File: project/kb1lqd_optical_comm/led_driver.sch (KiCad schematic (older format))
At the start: 0 parts

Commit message: Updated with better values and text.
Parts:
- added C?: 3.9n, symbol Device:C
- added Q?: PMBT2222AYS, Package_TO_SOT_SMD:SOT-363_SC-70-6, symbol Transistor_BJT:PMBT2222AYS
- added R?: 10k, symbol Device:R_US
- added R? (x2): 3.2k, symbol Device:R_US
- added R?: 1k, symbol Device:R_US
- added R?: 140, symbol Device:R_US
- added U?: AD8648, symbol kb1lqd_optical_comm:AD8648
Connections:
- net labels added: +5V, GND
- wire segments 0 -> 20
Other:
- note added: "1.2V Reference"
- note added: "LED DRIVE OUTPUT"
- note added: "UPDATED TO PMBF170 NMOS"
- note added: "fc(3dB)= x"
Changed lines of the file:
@@
 $Descr A4 11693 8268
 encoding utf-8
-Sheet 3 4
+Sheet 2 4
 Title ""
 Date ""
@@
 Comment4 ""
 $EndDescr
-Text HLabel 1800 2400 0    50   Input Italic 10
+Text HLabel 2050 3750 0    50   Input Italic 10
 AUDIO_INPUT
-Text HLabel 7050 2350 0    50   Input Italic 10
+Text HLabel 6950 2100 2    50   Input Italic 10
 LED_DRV
-Text HLabel 7050 2650 0    50   Input Italic 10
+Text HLabel 6950 2500 2    50   Input Italic 10
 LED_RTN
+$Comp
+L kb1lqd_optical_comm:AD8648 U?
+U 2 1 5F682513
+P 4900 3250
+F 0 "U?" H 5550 3283 50  0000 C CNN
+F 1 "AD8648" H 5550 3374 50  0000 C CNN
+F 2 "" H 4900 3250 50  0001 C CNN
+F 3 "" H 4900 3250 50  0001 C CNN
+	2    4900 3250
+	1    0    0    1
+$EndComp
+$Comp
+L Device:R_US R?
+U 1 1 5F6830F5
+P 2500 3750
+F 0 "R?" V 2295 3750 50  0000 C CNN
+F 1 "10k" V 2386 3750 50  0000 C CNN
+F 2 "" V 2540 3740 50  0001 C CNN
+F 3 "~" H 2500 3750 50  0001 C CNN
+	1    2500 3750
+	0    1    1    0
+$EndComp
+$Comp
+L Device:R_US R?
+U 1 1 5F684468
+P 4350 2950
+F 0 "R?" H 4418 2996 50  0000 L CNN
+F 1 "3.2k" H 4418 2905 50  0000 L CNN
+F 2 "" V 4390 2940 50  0001 C CNN
+F 3 "~" H 4350 2950 50  0001 C CNN
+	1    4350 2950
+	1    0    0    -1
+$EndComp
+Wire Wire Line
+	2350 3750 2050 3750
+Wire Wire Line
+	2650 3750 2900 3750
+Wire Wire Line
+	2900 3750 2900 3850
+Wire Wire Line
+	2900 4150 2900 4450
+Wire Wire Line
+	4350 3100 4350 3750
+Wire Wire Line
+	4350 4350 4350 4450
+Wire Wire Line
+	4350 2800 4350 2650
+$Comp
+L Device:R_US R?
+U 1 1 5F684893
+P 4350 4200
+F 0 "R?" H 4418 4246 50  0000 L CNN
+F 1 "1k" H 4418 4155 50  0000 L CNN
+F 2 "" V 4390 4190 50  0001 C CNN
+F 3 "~" H 4350 4200 50  0001 C CNN
+	1    4350 4200
+	1    0    0    -1
+$EndComp
+$Comp
+L power:GND #PWR?
+U 1 1 5F68C24A
+P 6950 4450
+F 0 "#PWR?" H 6950 4200 50  0001 C CNN
+F 1 "GND" H 6955 4277 50  0000 C CNN
+F 2 "" H 6950 4450 50  0001 C CNN
+F 3 "" H 6950 4450 50  0001 C CNN
+	1    6950 4450
+	1    0    0    -1
+$EndComp
+$Comp
+L power:GND #PWR?
+U 1 1 5F68C502
+P 2900 4450
+F 0 "#PWR?" H 2900 4200 50  0001 C CNN
+F 1 "GND" H 2905 4277 50  0000 C CNN
+F 2 "" H 2900 4450 50  0001 C CNN
+F 3 "" H 2900 4450 50  0001 C CNN
+	1    2900 4450
+	1    0    0    -1
+$EndComp
+$Comp
+L power:+5V #PWR?
+U 1 1 5F68CB23
+P 4350 2650
+F 0 "#PWR?" H 4350 2500 50  0001 C CNN
+F 1 "+5V" H 4365 2823 50  0000 C CNN
+F 2 "" H 4350 2650 50  0001 C CNN
+F 3 "" H 4350 2650 50  0001 C CNN
+	1    4350 2650
+	1    0    0    -1
+$EndComp
+Connection ~ 2900 3750
+Connection ~ 4350 3750
+Wire Wire Line
+	4350 3750 4350 4050
+Wire Wire Line
+	4350 3750 5250 3750
+$Comp
+L Transistor_BJT:PMBT2222AYS Q?
+U 1 1 5F6932D5
+P 6850 3650
+F 0 "Q?" H 7041 3696 50  0000 L CNN
+F 1 "PMBT2222AYS" H 7041 3605 50  0000 L CNN
+F 2 "Package_TO_SOT_SMD:SOT-363_SC-70-6" H 7050 3750 50  0001 C CNN
+F 3 "https://assets.nexperia.com/documents/data-sheet/PMBT2222AYS.pdf" H 6850 3650 50  0001 C CNN
+	1    6850 3650
+	1    0    0    -1
+$EndComp
+Wire Wire Line
+	5850 3650 6650 3650
+Wire Wire Line
+	6950 3450 6950 2900
+Wire Wire Line
+	6950 2900 5850 2900
+Wire Wire Line
+	5050 2900 5050 3550
+Wire Wire Line
+	5050 3550 5250 3550
+$Comp
+L Device:R_US R?
+U 1 1 5F6951A2
+P 5700 2900
+F 0 "R?" V 5495 2900 50  0000 C CNN
+F 1 "3.2k" V 5586 2900 50  0000 C CNN
+F 2 "" V 5740 2890 50  0001 C CNN
+F 3 "~" H 5700 2900 50  0001 C CNN
+	1    5700 2900
+	0    1    1    0
+$EndComp
+Wire Wire Line
+	5550 2900 5050 2900
+Text Notes 7050 3400 0    50   Italic 10
+UPDATED TO PMBF170 NMOS
+Wire Wire Line
+	6950 2900 6950 2500
+Connection ~ 6950 2900
+Wire Wire Line
+	6950 2100 6950 1550
+$Comp
+L power:+5V #PWR?
+U 1 1 5F69BF76
+P 6950 1550
+F 0 "#PWR?" H 6950 1400 50  0001 C CNN
+F 1 "+5V" H 6965 1723 50  0000 C CNN
+F 2 "" H 6950 1550 50  0001 C CNN
+F 3 "" H 6950 1550 50  0001 C CNN
+	1    6950 1550
+	1    0    0    -1
+$EndComp
+$Comp
+L Device:R_US R?
+U 1 1 5F69D7D6
+P 6950 4150
+F 0 "R?" H 7018 4196 50  0000 L CNN
+F 1 "140" H 7018 4105 50  0000 L CNN
+F 2 "" V 6990 4140 50  0001 C CNN
+F 3 "~" H 6950 4150 50  0001 C CNN
+	1    6950 4150
+	1    0    0    -1
+$EndComp
+Wire Wire Line
+	6950 4000 6950 3850
+Wire Wire Line
+	6950 4300 6950 4450
+$Comp
+L power:GND #PWR?
+U 1 1 5F6A2946
+P 4350 4450
+F 0 "#PWR?" H 4350 4200 50  0001 C CNN
+F 1 "GND" H 4355 4277 50  0000 C CNN
+F 2 "" H 4350 4450 50  0001 C CNN
+F 3 "" H 4350 4450 50  0001 C CNN
+	1    4350 4450
+	1    0    0    -1
+$EndComp
+Text Notes 7350 2350 0    50   Italic 10
+LED DRIVE OUTPUT
+Text Notes 4400 3400 0    50   Italic 10
+1.2V Reference
+Text Notes 2700 3450 0    50   Italic 10
+fc(3dB)= x
+Wire Wire Line
+	2900 3750 4350 3750
+$Comp
+L Device:C C?
+U 1 1 5F6D0D8B
+P 2900 4000
+F 0 "C?" H 3015 4046 50  0000 L CNN
+F 1 "3.9n" H 3015 3955 50  0000 L CNN
+F 2 "" H 2938 3850 50  0001 C CNN
+F 3 "~" H 2900 4000 50  0001 C CNN
+	1    2900 4000
+	1    0    0    -1
+$EndComp
 $EndSCHEMATC

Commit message: Adding updates.
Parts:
- removed Q?: PMBT2222AYS, Package_TO_SOT_SMD:SOT-363_SC-70-6, symbol Transistor_BJT:PMBT2222AYS
- added Q?: PMBF170, symbol kb1lqd_optical_comm:PMBF170
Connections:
- wire segments 20 -> 24
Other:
- note added: "Current Limit / Sense Resistor\nI(max) = 18mA"
- note added: "Id(max)=300mA\nPd(Max)=830mW\nRds(on)=5 Ohms\nRth(j-a)= 350 K/W"
- note removed: "UPDATED TO PMBF170 NMOS"
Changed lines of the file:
@@
 Text HLabel 2050 3750 0    50   Input Italic 10
 AUDIO_INPUT
-Text HLabel 6950 2100 2    50   Input Italic 10
+Text HLabel 7350 2100 2    50   Input Italic 10
 LED_DRV
-Text HLabel 6950 2500 2    50   Input Italic 10
+Text HLabel 7350 2500 2    50   Input Italic 10
 LED_RTN
 $Comp
@@
 Wire Wire Line
 	4350 3750 5250 3750
-$Comp
-L Transistor_BJT:PMBT2222AYS Q?
-U 1 1 5F6932D5
-P 6850 3650
-F 0 "Q?" H 7041 3696 50  0000 L CNN
-F 1 "PMBT2222AYS" H 7041 3605 50  0000 L CNN
-F 2 "Package_TO_SOT_SMD:SOT-363_SC-70-6" H 7050 3750 50  0001 C CNN
-F 3 "https://assets.nexperia.com/documents/data-sheet/PMBT2222AYS.pdf" H 6850 3650 50  0001 C CNN
-	1    6850 3650
-	1    0    0    -1
-$EndComp
 Wire Wire Line
 	5850 3650 6650 3650
-Wire Wire Line
-	6950 3450 6950 2900
-Wire Wire Line
-	6950 2900 5850 2900
 Wire Wire Line
 	5050 2900 5050 3550
@@
 Wire Wire Line
 	5550 2900 5050 2900
-Text Notes 7050 3400 0    50   Italic 10
-UPDATED TO PMBF170 NMOS
-Wire Wire Line
-	6950 2900 6950 2500
-Connection ~ 6950 2900
 Wire Wire Line
 	6950 2100 6950 1550
@@
 $EndComp
 Wire Wire Line
-	6950 4000 6950 3850
+	6950 4000 6950 3950
 Wire Wire Line
 	6950 4300 6950 4450
@@
 	1    0    0    -1
 $EndComp
-Text Notes 7350 2350 0    50   Italic 10
+Text Notes 7350 2350 0    50   ~ 0
 LED DRIVE OUTPUT
-Text Notes 4400 3400 0    50   Italic 10
+Text Notes 4500 3700 0    50   ~ 0
 1.2V Reference
 Text Notes 2700 3450 0    50   Italic 10
@@
 	1    0    0    -1
 $EndComp
+$Comp
+L kb1lqd_optical_comm:PMBF170 Q?
+U 1 1 5F6ED2B2
+P 6450 4100
+F 0 "Q?" H 7055 4596 50  0000 L CNN
+F 1 "PMBF170" H 7055 4505 50  0000 L CNN
+F 2 "" H 6450 4100 50  0001 C CNN
+F 3 "" H 6450 4100 50  0001 C CNN
+	1    6450 4100
+	1    0    0    -1
+$EndComp
+Text Notes 7600 3800 0    50   ~ 0
+Id(max)=300mA\nPd(Max)=830mW\nRds(on)=5 Ohms\nRth(j-a)= 350 K/W
+Text Notes 7600 4250 0    50   ~ 0
+Current Limit / Sense Resistor\nI(max) = 18mA
+Wire Wire Line
+	6950 2500 6950 3450
+Wire Wire Line
+	7450 2900 7450 3950
+Wire Wire Line
+	7450 3950 6950 3950
+Wire Wire Line
+	5850 2900 7450 2900
+Connection ~ 6950 3950
+Wire Wire Line
+	6950 3950 6950 3850
+Wire Wire Line
+	6950 2100 7350 2100
+Wire Wire Line
+	6950 2500 7350 2500
 $EndSCHEMATC

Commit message: Schematic essentially done.
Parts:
- gave numbers to parts that had none: 8
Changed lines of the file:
@@
 $Descr A4 11693 8268
 encoding utf-8
-Sheet 2 5
+Sheet 2 6
 Title ""
 Date ""
@@
 LED_RTN
 $Comp
-L kb1lqd_optical_comm:AD8648 U?
+L kb1lqd_optical_comm:AD8648 U1
 U 2 1 5F682513
 P 4900 3250
-F 0 "U?" H 5550 3283 50  0000 C CNN
+F 0 "U1" H 5550 3283 50  0000 C CNN
 F 1 "AD8648" H 5550 3374 50  0000 C CNN
 F 2 "" H 4900 3250 50  0001 C CNN
@@
 $EndComp
 $Comp
-L Device:R_US R?
+L Device:R_US R8
 U 1 1 5F6830F5
 P 2500 3750
-F 0 "R?" V 2295 3750 50  0000 C CNN
+F 0 "R8" V 2295 3750 50  0000 C CNN
 F 1 "10k" V 2386 3750 50  0000 C CNN
 F 2 "" V 2540 3740 50  0001 C CNN
@@
 $EndComp
 $Comp
-L Device:R_US R?
+L Device:R_US R9
 U 1 1 5F684468
 P 4350 2950
-F 0 "R?" H 4418 2996 50  0000 L CNN
+F 0 "R9" H 4418 2996 50  0000 L CNN
 F 1 "3.2k" H 4418 2905 50  0000 L CNN
 F 2 "" V 4390 2940 50  0001 C CNN
@@
 	4350 2800 4350 2650
 $Comp
-L Device:R_US R?
+L Device:R_US R10
 U 1 1 5F684893
 P 4350 4200
-F 0 "R?" H 4418 4246 50  0000 L CNN
+F 0 "R10" H 4418 4246 50  0000 L CNN
 F 1 "1k" H 4418 4155 50  0000 L CNN
 F 2 "" V 4390 4190 50  0001 C CNN
@@
 $EndComp
 $Comp
-L power:GND #PWR?
+L power:GND #PWR012
 U 1 1 5F68C24A
 P 6950 4450
-F 0 "#PWR?" H 6950 4200 50  0001 C CNN
+F 0 "#PWR012" H 6950 4200 50  0001 C CNN
 F 1 "GND" H 6955 4277 50  0000 C CNN
 F 2 "" H 6950 4450 50  0001 C CNN
@@
 $EndComp
 $Comp
-L power:GND #PWR?
+L power:GND #PWR08
 U 1 1 5F68C502
 P 2900 4450
-F 0 "#PWR?" H 2900 4200 50  0001 C CNN
+F 0 "#PWR08" H 2900 4200 50  0001 C CNN
 F 1 "GND" H 2905 4277 50  0000 C CNN
 F 2 "" H 2900 4450 50  0001 C CNN
@@
 $EndComp
 $Comp
-L power:+5V #PWR?
+L power:+5V #PWR09
 U 1 1 5F68CB23
 P 4350 2650
-F 0 "#PWR?" H 4350 2500 50  0001 C CNN
+F 0 "#PWR09" H 4350 2500 50  0001 C CNN
 F 1 "+5V" H 4365 2823 50  0000 C CNN
 F 2 "" H 4350 2650 50  0001 C CNN
@@
 	5050 3550 5250 3550
 $Comp
-L Device:R_US R?
+L Device:R_US R11
 U 1 1 5F6951A2
 P 5700 2900
-F 0 "R?" V 5495 2900 50  0000 C CNN
+F 0 "R11" V 5495 2900 50  0000 C CNN
 F 1 "3.2k" V 5586 2900 50  0000 C CNN
 F 2 "" V 5740 2890 50  0001 C CNN
@@
 	6950 2100 6950 1550
 $Comp
-L power:+5V #PWR?
+L power:+5V #PWR011
 U 1 1 5F69BF76
 P 6950 1550
-F 0 "#PWR?" H 6950 1400 50  0001 C CNN
+F 0 "#PWR011" H 6950 1400 50  0001 C CNN
 F 1 "+5V" H 6965 1723 50  0000 C CNN
 F 2 "" H 6950 1550 50  0001 C CNN
@@
 $EndComp
 $Comp
-L Device:R_US R?
+L Device:R_US R12
 U 1 1 5F69D7D6
 P 6950 4150
-F 0 "R?" H 7018 4196 50  0000 L CNN
+F 0 "R12" H 7018 4196 50  0000 L CNN
 F 1 "140" H 7018 4105 50  0000 L CNN
 F 2 "" V 6990 4140 50  0001 C CNN
@@
 	6950 4300 6950 4450
 $Comp
-L power:GND #PWR?
+L power:GND #PWR010
 U 1 1 5F6A2946
 P 4350 4450
-F 0 "#PWR?" H 4350 4200 50  0001 C CNN
+F 0 "#PWR010" H 4350 4200 50  0001 C CNN
 F 1 "GND" H 4355 4277 50  0000 C CNN
 F 2 "" H 4350 4450 50  0001 C CNN
@@
 	2900 3750 4350 3750
 $Comp
-L Device:C C?
+L Device:C C1
 U 1 1 5F6D0D8B
 P 2900 4000
-F 0 "C?" H 3015 4046 50  0000 L CNN
+F 0 "C1" H 3015 4046 50  0000 L CNN
 F 1 "3.9n" H 3015 3955 50  0000 L CNN
 F 2 "" H 2938 3850 50  0001 C CNN
@@
 $EndComp
 $Comp
-L kb1lqd_optical_comm:PMBF170 Q?
+L kb1lqd_optical_comm:PMBF170 Q1
 U 1 1 5F6ED2B2
 P 6450 4100
-F 0 "Q?" H 7055 4596 50  0000 L CNN
+F 0 "Q1" H 7055 4596 50  0000 L CNN
 F 1 "PMBF170" H 7055 4505 50  0000 L CNN
 F 2 "" H 6450 4100 50  0001 C CNN

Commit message: Updated with all footprints
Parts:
- C1: footprint (none) -> Capacitor_SMD:C_0805_2012Metric
- Q1: footprint (none) -> Package_TO_SOT_SMD:SOT-23
- R10, R11, R12, R8, R9: footprint (none) -> Resistor_SMD:R_0603_1608Metric
- U1: footprint (none) -> Package_SO:TSSOP-14_4.4x5mm_P0.65mm
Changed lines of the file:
@@
 F 0 "U1" H 5550 3283 50  0000 C CNN
 F 1 "AD8648" H 5550 3374 50  0000 C CNN
-F 2 "" H 4900 3250 50  0001 C CNN
+F 2 "Package_SO:TSSOP-14_4.4x5mm_P0.65mm" H 4900 3250 50  0001 C CNN
 F 3 "" H 4900 3250 50  0001 C CNN
 	2    4900 3250
@@
 F 0 "R8" V 2295 3750 50  0000 C CNN
 F 1 "10k" V 2386 3750 50  0000 C CNN
-F 2 "" V 2540 3740 50  0001 C CNN
+F 2 "Resistor_SMD:R_0603_1608Metric" V 2540 3740 50  0001 C CNN
 F 3 "~" H 2500 3750 50  0001 C CNN
 	1    2500 3750
@@
 F 0 "R9" H 4418 2996 50  0000 L CNN
 F 1 "3.2k" H 4418 2905 50  0000 L CNN
-F 2 "" V 4390 2940 50  0001 C CNN
+F 2 "Resistor_SMD:R_0603_1608Metric" V 4390 2940 50  0001 C CNN
 F 3 "~" H 4350 2950 50  0001 C CNN
 	1    4350 2950
@@
 F 0 "R10" H 4418 4246 50  0000 L CNN
 F 1 "1k" H 4418 4155 50  0000 L CNN
-F 2 "" V 4390 4190 50  0001 C CNN
+F 2 "Resistor_SMD:R_0603_1608Metric" V 4390 4190 50  0001 C CNN
 F 3 "~" H 4350 4200 50  0001 C CNN
 	1    4350 4200
@@
 F 0 "R11" V 5495 2900 50  0000 C CNN
 F 1 "3.2k" V 5586 2900 50  0000 C CNN
-F 2 "" V 5740 2890 50  0001 C CNN
+F 2 "Resistor_SMD:R_0603_1608Metric" V 5740 2890 50  0001 C CNN
 F 3 "~" H 5700 2900 50  0001 C CNN
 	1    5700 2900
@@
 F 0 "R12" H 7018 4196 50  0000 L CNN
 F 1 "140" H 7018 4105 50  0000 L CNN
-F 2 "" V 6990 4140 50  0001 C CNN
+F 2 "Resistor_SMD:R_0603_1608Metric" V 6990 4140 50  0001 C CNN
 F 3 "~" H 6950 4150 50  0001 C CNN
 	1    6950 4150
@@
 F 0 "C1" H 3015 4046 50  0000 L CNN
 F 1 "3.9n" H 3015 3955 50  0000 L CNN
-F 2 "" H 2938 3850 50  0001 C CNN
+F 2 "Capacitor_SMD:C_0805_2012Metric" H 2938 3850 50  0001 C CNN
 F 3 "~" H 2900 4000 50  0001 C CNN
 	1    2900 4000
@@
 F 0 "Q1" H 7055 4596 50  0000 L CNN
 F 1 "PMBF170" H 7055 4505 50  0000 L CNN
-F 2 "" H 6450 4100 50  0001 C CNN
+F 2 "Package_TO_SOT_SMD:SOT-23" H 6450 4100 50  0001 C CNN
 F 3 "" H 6450 4100 50  0001 C CNN
 	1    6450 4100

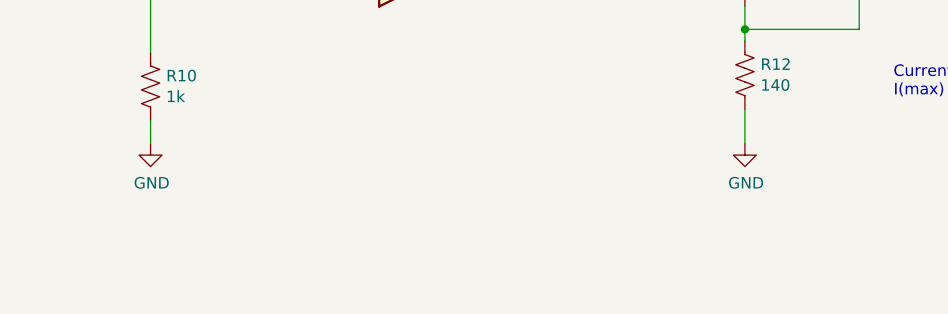
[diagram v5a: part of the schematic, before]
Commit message: Initial placement mostly done. Outlined PCB.
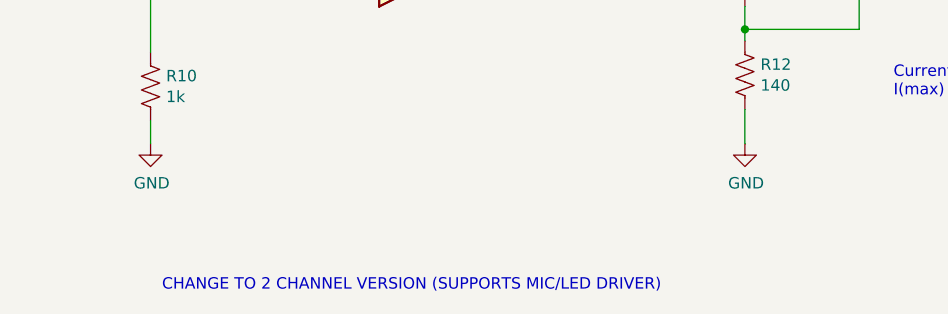
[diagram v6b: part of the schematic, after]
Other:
- note added: "CHANGE TO 2 CHANNEL VERSION (SUPPORTS MIC/LED DRIVER)"
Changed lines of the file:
@@
 Wire Wire Line
 	6950 2500 7350 2500
+Text Notes 4400 5100 0    50   ~ 0
+CHANGE TO 2 CHANNEL VERSION (SUPPORTS MIC/LED DRIVER)
 $EndSCHEMATC

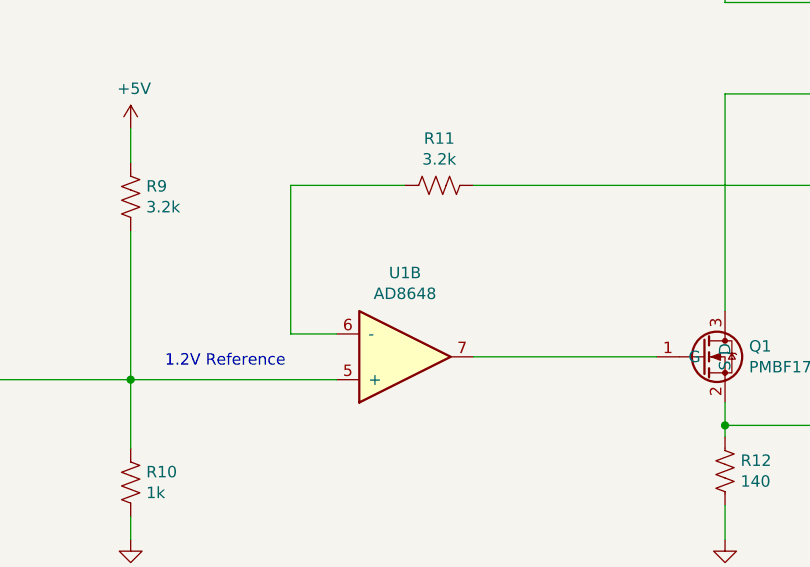
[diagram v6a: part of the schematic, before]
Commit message: Initial placement condensed.
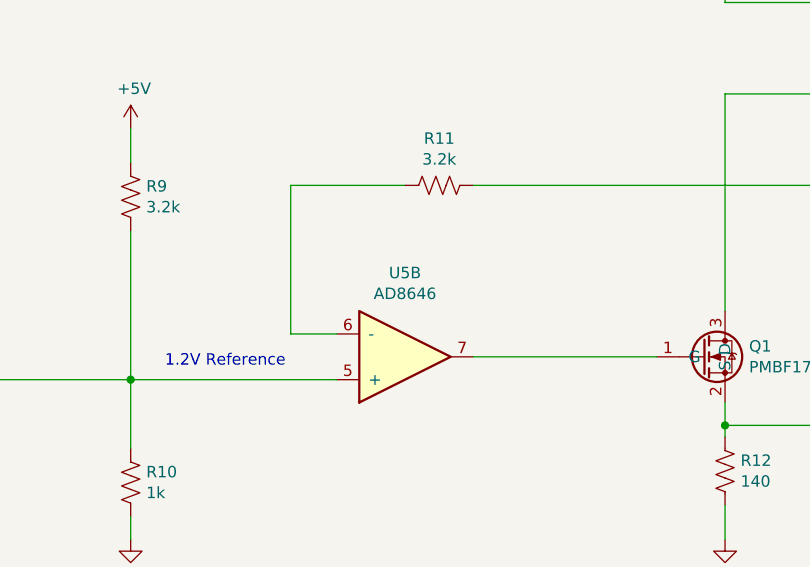
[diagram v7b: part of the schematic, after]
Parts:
- removed U1: AD8648, Package_SO:TSSOP-14_4.4x5mm_P0.65mm, symbol kb1lqd_optical_comm:AD8648
- added U5: AD8646, Package_SO:SOIC-8_3.9x4.9mm_P1.27mm, symbol kb1lqd_optical_comm:AD8646
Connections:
- net at C1.1, R10.1, R8.1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: now also U5.5 (+)
- net at R11.2: now also U5.6 (-)
- net at Q1.1 (G): now also U5.7
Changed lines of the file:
@@
 LED_RTN
-$Comp
-L kb1lqd_optical_comm:AD8648 U1
-U 2 1 5F682513
-P 4900 3250
-F 0 "U1" H 5550 3283 50  0000 C CNN
-F 1 "AD8648" H 5550 3374 50  0000 C CNN
-F 2 "Package_SO:TSSOP-14_4.4x5mm_P0.65mm" H 4900 3250 50  0001 C CNN
-F 3 "" H 4900 3250 50  0001 C CNN
-	2    4900 3250
-	1    0    0    1
-$EndComp
 $Comp
 L Device:R_US R8
@@
 Text Notes 4400 5100 0    50   ~ 0
 CHANGE TO 2 CHANNEL VERSION (SUPPORTS MIC/LED DRIVER)
+$Comp
+L kb1lqd_optical_comm:AD8646 U5
+U 2 1 5FEA66D4
+P 4900 3250
+F 0 "U5" H 5550 3283 50  0000 C CNN
+F 1 "AD8646" H 5550 3374 50  0000 C CNN
+F 2 "Package_SO:SOIC-8_3.9x4.9mm_P1.27mm" H 4900 3250 50  0001 C CNN
+F 3 "" H 4900 3250 50  0001 C CNN
+	2    4900 3250
+	1    0    0    1
+$EndComp
 $EndSCHEMATC
